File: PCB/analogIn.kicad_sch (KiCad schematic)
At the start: 8 parts

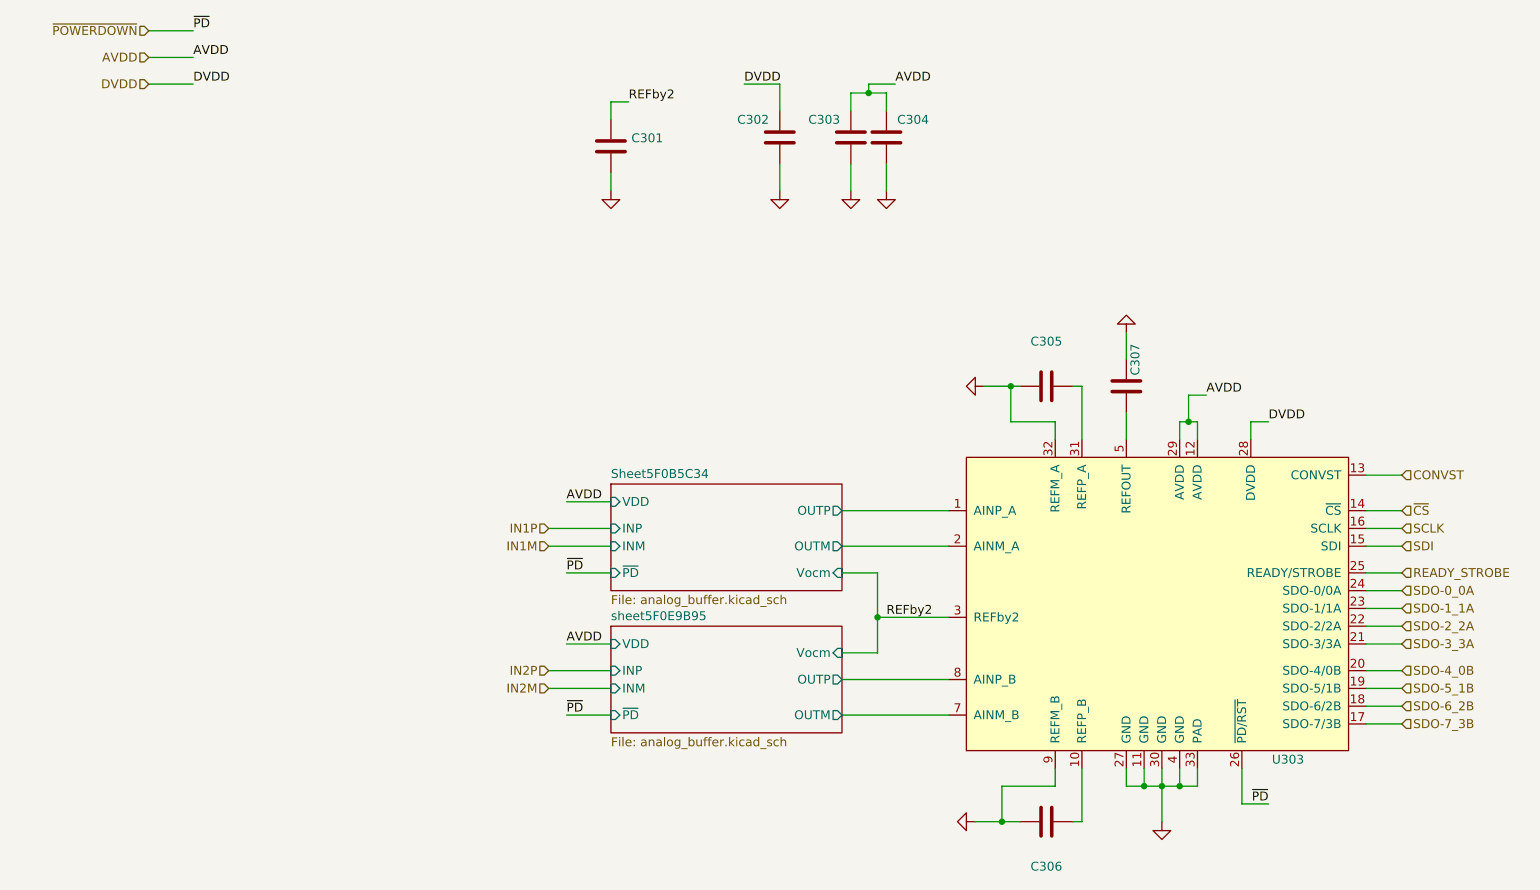
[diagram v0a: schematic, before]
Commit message: New version with FTDI chip instead of STM32 and ICE40HX FPGA instead of slower ones
Signed-off-by: Alexis Jeandet <alexis.jeandet@member.fsf.org>
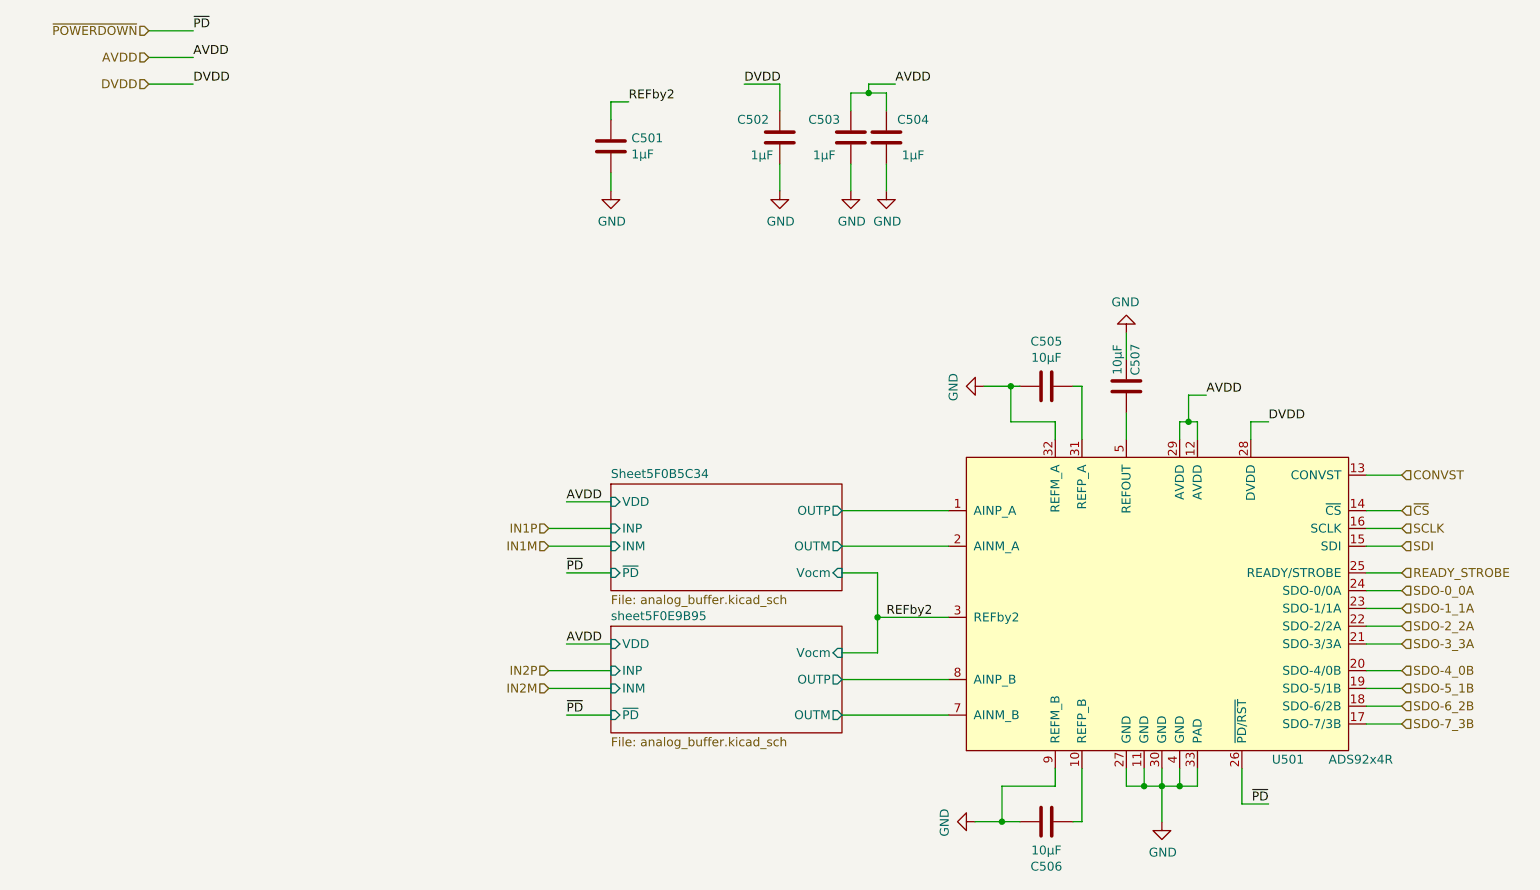
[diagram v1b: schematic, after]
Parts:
- C501: renamed from C301; value (none) -> 1µF; footprint (none) -> Capacitor_SMD:C_0805_2012Metric_Pad1.15x1.40mm_HandSolder
- C502: renamed from C302; value (none) -> 1µF; footprint (none) -> Capacitor_SMD:C_0805_2012Metric_Pad1.15x1.40mm_HandSolder
- C503: renamed from C303; value (none) -> 1µF; footprint (none) -> Capacitor_SMD:C_0805_2012Metric_Pad1.15x1.40mm_HandSolder
- C504: renamed from C304; value (none) -> 1µF; footprint (none) -> Capacitor_SMD:C_0805_2012Metric_Pad1.15x1.40mm_HandSolder
- C505: renamed from C305; value (none) -> 10µF; footprint (none) -> Capacitor_SMD:C_1206_3216Metric_Pad1.42x1.75mm_HandSolder
- C506: renamed from C306; value (none) -> 10µF; footprint (none) -> Capacitor_SMD:C_1206_3216Metric_Pad1.42x1.75mm_HandSolder
- C507: renamed from C307; value (none) -> 10µF; footprint (none) -> Capacitor_SMD:C_1206_3216Metric_Pad1.42x1.75mm_HandSolder
- U501: renamed from U303; value (none) -> ADS92x4R; footprint (none) -> Package_DFN_QFN:VQFN-32-1EP_5x5mm_P0.5mm_EP3.1x3.1mm
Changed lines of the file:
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@@
     (title "Dual chan ADC")
     (date "2020-09-21")
-    (rev "1.0")
+    (rev "1.1")
     (company "LPP/CNRS")
     (comment 1 "Alexis Jeandet")
@@
   (symbol (lib_id "ADS92x4R:ADS92x4R") (at 154.94 125.73 0) (unit 1)
     (in_bom yes) (on_board yes)
-    (property "Reference" "U303" (id 0) (at 203.2 127 0)
+    (property "Reference" "U501" (id 0) (at 203.2 127 0)
       (effects (font (size 1.27 1.27)) (justify right))
     )
-    (property "Value" "" (id 1) (at 215.9 127 0)
+    (property "Value" "ADS92x4R" (id 1) (at 215.9 127 0)
       (effects (font (size 1.27 1.27)) (justify right))
     )
-    (property "Footprint" "" (id 2) (at 154.94 125.73 0)
+    (property "Footprint" "Package_DFN_QFN:VQFN-32-1EP_5x5mm_P0.5mm_EP3.1x3.1mm" (id 2) (at 154.94 125.73 0)
       (effects (font (size 1.27 1.27)) hide)
     )
@@
   (symbol (lib_id "Device:C") (at 104.14 39.37 0) (unit 1)
     (in_bom yes) (on_board yes)
-    (property "Reference" "C301" (id 0) (at 107.061 38.2016 0)
+    (property "Reference" "C501" (id 0) (at 107.061 38.2016 0)
       (effects (font (size 1.27 1.27)) (justify left))
     )
-    (property "Value" "" (id 1) (at 107.061 40.513 0)
+    (property "Value" "1µF" (id 1) (at 107.061 40.513 0)
       (effects (font (size 1.27 1.27)) (justify left))
     )
-    (property "Footprint" "" (id 2) (at 105.1052 43.18 0)
+    (property "Footprint" "Capacitor_SMD:C_0805_2012Metric_Pad1.15x1.40mm_HandSolder" (id 2) (at 105.1052 43.18 0)
       (effects (font (size 1.27 1.27)) hide)
     )
@@
   (symbol (lib_id "power:GND") (at 104.14 45.72 0) (unit 1)
     (in_bom yes) (on_board yes)
-    (property "Reference" "#PWR0301" (id 0) (at 104.14 52.07 0)
-      (effects (font (size 1.27 1.27)) hide)
-    )
-    (property "Value" "" (id 1) (at 104.267 50.1142 0))
+    (property "Reference" "#PWR0501" (id 0) (at 104.14 52.07 0)
+      (effects (font (size 1.27 1.27)) hide)
+    )
+    (property "Value" "GND" (id 1) (at 104.267 50.1142 0))
     (property "Footprint" "" (id 2) (at 104.14 45.72 0)
       (effects (font (size 1.27 1.27)) hide)
@@
   (symbol (lib_id "Device:C") (at 166.37 73.66 90) (unit 1)
     (in_bom yes) (on_board yes)
-    (property "Reference" "C305" (id 0) (at 166.37 67.2592 90))
-    (property "Value" "" (id 1) (at 166.37 69.5706 90))
-    (property "Footprint" "" (id 2) (at 170.18 72.6948 0)
+    (property "Reference" "C505" (id 0) (at 166.37 67.2592 90))
+    (property "Value" "10µF" (id 1) (at 166.37 69.5706 90))
+    (property "Footprint" "Capacitor_SMD:C_1206_3216Metric_Pad1.42x1.75mm_HandSolder" (id 2) (at 170.18 72.6948 0)
       (effects (font (size 1.27 1.27)) hide)
     )
@@
   (symbol (lib_id "Device:C") (at 166.37 135.89 270) (unit 1)
     (in_bom yes) (on_board yes)
-    (property "Reference" "C306" (id 0) (at 166.37 142.2908 90))
-    (property "Value" "" (id 1) (at 166.37 139.9794 90))
-    (property "Footprint" "" (id 2) (at 162.56 136.8552 0)
+    (property "Reference" "C506" (id 0) (at 166.37 142.2908 90))
+    (property "Value" "10µF" (id 1) (at 166.37 139.9794 90))
+    (property "Footprint" "Capacitor_SMD:C_1206_3216Metric_Pad1.42x1.75mm_HandSolder" (id 2) (at 162.56 136.8552 0)
       (effects (font (size 1.27 1.27)) hide)
     )
@@
   (symbol (lib_id "power:GND") (at 157.48 73.66 270) (unit 1)
     (in_bom yes) (on_board yes)
-    (property "Reference" "#PWR0304" (id 0) (at 151.13 73.66 0)
-      (effects (font (size 1.27 1.27)) hide)
-    )
-    (property "Value" "" (id 1) (at 153.0858 73.787 0))
+    (property "Reference" "#PWR0506" (id 0) (at 151.13 73.66 0)
+      (effects (font (size 1.27 1.27)) hide)
+    )
+    (property "Value" "GND" (id 1) (at 153.0858 73.787 0))
     (property "Footprint" "" (id 2) (at 157.48 73.66 0)
       (effects (font (size 1.27 1.27)) hide)
@@
   (symbol (lib_id "power:GND") (at 156.21 135.89 270) (unit 1)
     (in_bom yes) (on_board yes)
-    (property "Reference" "#PWR0303" (id 0) (at 149.86 135.89 0)
-      (effects (font (size 1.27 1.27)) hide)
-    )
-    (property "Value" "" (id 1) (at 151.8158 136.017 0))
+    (property "Reference" "#PWR0505" (id 0) (at 149.86 135.89 0)
+      (effects (font (size 1.27 1.27)) hide)
+    )
+    (property "Value" "GND" (id 1) (at 151.8158 136.017 0))
     (property "Footprint" "" (id 2) (at 156.21 135.89 0)
       (effects (font (size 1.27 1.27)) hide)
@@
   (symbol (lib_id "Device:C") (at 177.8 73.66 0) (unit 1)
     (in_bom yes) (on_board yes)
-    (property "Reference" "C307" (id 0) (at 179.07 69.85 90))
-    (property "Value" "" (id 1) (at 176.53 69.85 90))
-    (property "Footprint" "" (id 2) (at 178.7652 77.47 0)
+    (property "Reference" "C507" (id 0) (at 179.07 69.85 90))
+    (property "Value" "10µF" (id 1) (at 176.53 69.85 90))
+    (property "Footprint" "Capacitor_SMD:C_1206_3216Metric_Pad1.42x1.75mm_HandSolder" (id 2) (at 178.7652 77.47 0)
       (effects (font (size 1.27 1.27)) hide)
     )
@@
   (symbol (lib_id "power:GND") (at 177.8 66.04 180) (unit 1)
     (in_bom yes) (on_board yes)
-    (property "Reference" "#PWR0307" (id 0) (at 177.8 59.69 0)
-      (effects (font (size 1.27 1.27)) hide)
-    )
-    (property "Value" "" (id 1) (at 177.673 61.6458 0))
+    (property "Reference" "#PWR0507" (id 0) (at 177.8 59.69 0)
+      (effects (font (size 1.27 1.27)) hide)
+    )
+    (property "Value" "GND" (id 1) (at 177.673 61.6458 0))
     (property "Footprint" "" (id 2) (at 177.8 66.04 0)
       (effects (font (size 1.27 1.27)) hide)
@@
   (symbol (lib_id "Device:C") (at 143.51 38.1 180) (unit 1)
     (in_bom yes) (on_board yes)
-    (property "Reference" "C304" (id 0) (at 147.32 35.56 0))
-    (property "Value" "" (id 1) (at 147.32 40.64 0))
-    (property "Footprint" "" (id 2) (at 142.5448 34.29 0)
+    (property "Reference" "C504" (id 0) (at 147.32 35.56 0))
+    (property "Value" "1µF" (id 1) (at 147.32 40.64 0))
+    (property "Footprint" "Capacitor_SMD:C_0805_2012Metric_Pad1.15x1.40mm_HandSolder" (id 2) (at 142.5448 34.29 0)
       (effects (font (size 1.27 1.27)) hide)
     )
@@
   (symbol (lib_id "Device:C") (at 138.43 38.1 180) (unit 1)
     (in_bom yes) (on_board yes)
-    (property "Reference" "C303" (id 0) (at 134.62 35.56 0))
-    (property "Value" "" (id 1) (at 134.62 40.64 0))
-    (property "Footprint" "" (id 2) (at 137.4648 34.29 0)
+    (property "Reference" "C503" (id 0) (at 134.62 35.56 0))
+    (property "Value" "1µF" (id 1) (at 134.62 40.64 0))
+    (property "Footprint" "Capacitor_SMD:C_0805_2012Metric_Pad1.15x1.40mm_HandSolder" (id 2) (at 137.4648 34.29 0)
       (effects (font (size 1.27 1.27)) hide)
     )
@@
   (symbol (lib_id "power:GND") (at 143.51 45.72 0) (unit 1)
     (in_bom yes) (on_board yes)
-    (property "Reference" "#PWR0306" (id 0) (at 143.51 52.07 0)
-      (effects (font (size 1.27 1.27)) hide)
-    )
-    (property "Value" "" (id 1) (at 143.637 50.1142 0))
+    (property "Reference" "#PWR0504" (id 0) (at 143.51 52.07 0)
+      (effects (font (size 1.27 1.27)) hide)
+    )
+    (property "Value" "GND" (id 1) (at 143.637 50.1142 0))
     (property "Footprint" "" (id 2) (at 143.51 45.72 0)
       (effects (font (size 1.27 1.27)) hide)
@@
   (symbol (lib_id "power:GND") (at 138.43 45.72 0) (unit 1)
     (in_bom yes) (on_board yes)
-    (property "Reference" "#PWR0305" (id 0) (at 138.43 52.07 0)
-      (effects (font (size 1.27 1.27)) hide)
-    )
-    (property "Value" "" (id 1) (at 138.557 50.1142 0))
+    (property "Reference" "#PWR0503" (id 0) (at 138.43 52.07 0)
+      (effects (font (size 1.27 1.27)) hide)
+    )
+    (property "Value" "GND" (id 1) (at 138.557 50.1142 0))
     (property "Footprint" "" (id 2) (at 138.43 45.72 0)
       (effects (font (size 1.27 1.27)) hide)
@@
   (symbol (lib_id "Device:C") (at 128.27 38.1 180) (unit 1)
     (in_bom yes) (on_board yes)
-    (property "Reference" "C302" (id 0) (at 124.46 35.56 0))
-    (property "Value" "" (id 1) (at 125.73 40.64 0))
-    (property "Footprint" "" (id 2) (at 127.3048 34.29 0)
+    (property "Reference" "C502" (id 0) (at 124.46 35.56 0))
+    (property "Value" "1µF" (id 1) (at 125.73 40.64 0))
+    (property "Footprint" "Capacitor_SMD:C_0805_2012Metric_Pad1.15x1.40mm_HandSolder" (id 2) (at 127.3048 34.29 0)
       (effects (font (size 1.27 1.27)) hide)
     )
@@
   (symbol (lib_id "power:GND") (at 128.27 45.72 0) (unit 1)
     (in_bom yes) (on_board yes)
-    (property "Reference" "#PWR0302" (id 0) (at 128.27 52.07 0)
-      (effects (font (size 1.27 1.27)) hide)
-    )
-    (property "Value" "" (id 1) (at 128.397 50.1142 0))
+    (property "Reference" "#PWR0502" (id 0) (at 128.27 52.07 0)
+      (effects (font (size 1.27 1.27)) hide)
+    )
+    (property "Value" "GND" (id 1) (at 128.397 50.1142 0))
     (property "Footprint" "" (id 2) (at 128.27 45.72 0)
       (effects (font (size 1.27 1.27)) hide)
@@
   (symbol (lib_id "power:GND") (at 182.88 135.89 0) (unit 1)
     (in_bom yes) (on_board yes)
-    (property "Reference" "#PWR0308" (id 0) (at 182.88 142.24 0)
-      (effects (font (size 1.27 1.27)) hide)
-    )
-    (property "Value" "" (id 1) (at 183.007 140.2842 0))
+    (property "Reference" "#PWR0508" (id 0) (at 182.88 142.24 0)
+      (effects (font (size 1.27 1.27)) hide)
+    )
+    (property "Value" "GND" (id 1) (at 183.007 140.2842 0))
     (property "Footprint" "" (id 2) (at 182.88 135.89 0)
       (effects (font (size 1.27 1.27)) hide)
